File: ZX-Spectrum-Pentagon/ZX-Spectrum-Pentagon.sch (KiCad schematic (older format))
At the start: 0 parts

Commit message: improve Video_Formating
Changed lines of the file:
@@
 	7000 6500 5000 6500
 Connection ~ 5000 6500
-Wire Bus Line
-	5000 6500 5000 7750
 Wire Wire Line
 	6500 1550 6900 1550
@@
 $EndSheet
 $Sheet
-S 3500 5400 1000 2250
+S 3500 5400 1000 2200
 U 62FD43AB
 F0 "VideoFormating" 50
@@
 F8 "MD6" I L 3500 6100 50
 F9 "MD7" I L 3500 6200 50
-F10 "CBER0" I L 3500 6400 50
+F10 "CBRD0" I L 3500 6400 50
 F11 "CBRD1" I L 3500 6500 50
 F12 "CBRD2" I L 3500 6600 50
@@
 F14 "~C2" I L 3500 7000 50
 F15 "C3" I L 3500 7100 50
-F16 "C17" I L 3500 7300 50
-F17 "C18" I L 3500 7400 50
-F18 "BL" I L 3500 7500 50
+F16 "C17" I L 3500 7400 50
+F17 "C18" I L 3500 7500 50
+F18 "BL" I R 4500 7500 50
 F19 "RED" O R 4500 5600 50
 F20 "GREEN" O R 4500 5700 50
 F21 "BLUE" O R 4500 5800 50
-F22 "SYNCOUT" O R 4500 5900 50
-F23 "SYNC" O R 4500 6000 50
+F22 "SYNCOUT" O R 4500 6650 50
+F23 "SYNC" O R 4500 6750 50
 F24 "F-25Hz" I L 3500 6300 50
 F25 "PA6" I L 3500 6700 50
 F26 "PA7" I L 3500 6800 50
 F27 "C5" I L 3500 7200 50
-F28 "GPA6" O R 4500 6100 50
-F29 "GPA7" O R 4500 6200 50
+F28 "GPA6" O R 4500 7100 50
+F29 "GPA7" O R 4500 7200 50
+F30 "C7" I L 3500 7300 50
 $EndSheet
 Wire Wire Line
@@
 C3
 Text Label 3100 7300 0    50   ~ 0
+C7
+Text Label 3100 7400 0    50   ~ 0
 C17
-Text Label 3100 7400 0    50   ~ 0
+Text Label 3100 7500 0    50   ~ 0
 C18
-Text Label 3100 7500 0    50   ~ 0
-BL
 Entry Wire Line
 	5000 5700 4900 5600
@@
 	5000 5900 4900 5800
 Entry Wire Line
-	5000 6000 4900 5900
-Entry Wire Line
-	5000 6100 4900 6000
+	5000 6750 4900 6650
+Entry Wire Line
+	5000 6850 4900 6750
 Wire Wire Line
 	4900 5600 4500 5600
@@
 	4900 5800 4500 5800
 Wire Wire Line
-	4900 5900 4500 5900
-Wire Wire Line
-	4900 6000 4500 6000
+	4900 6650 4500 6650
+Wire Wire Line
+	4900 6750 4500 6750
 Text Label 4900 5600 2    50   ~ 0
 RED
@@
 Text Label 4900 5800 2    50   ~ 0
 BLUE
-Text Label 4900 5900 2    50   ~ 0
+Text Label 4900 6650 2    50   ~ 0
 SYNCOUT
-Text Label 4900 6000 2    50   ~ 0
+Text Label 4900 6750 2    50   ~ 0
 SYNC
 Entry Wire Line
@@
 C5
 Entry Wire Line
-	4900 6100 5000 6200
-Entry Wire Line
-	4900 6200 5000 6300
-Wire Wire Line
-	4500 6100 4900 6100
-Wire Wire Line
-	4500 6200 4900 6200
+	4900 7100 5000 7200
+Entry Wire Line
+	4900 7200 5000 7300
+Wire Wire Line
+	4500 7100 4900 7100
+Wire Wire Line
+	4500 7200 4900 7200
+Text Label 4900 7100 2    50   ~ 0
+GPA6
+Text Label 4900 7200 2    50   ~ 0
+GPA7
+Entry Wire Line
+	4900 7500 5000 7600
+Wire Wire Line
+	4500 7500 4900 7500
+Text Label 4900 7500 2    50   ~ 0
+BL
+Wire Bus Line
+	5000 6500 5000 7750
 Wire Bus Line
 	1000 900  1000 7750
@@
 Wire Bus Line
 	3000 800  3000 7750
-Text Label 4900 6100 2    50   ~ 0
-GPA6
-Text Label 4900 6200 2    50   ~ 0
-GPA7
 $EndSCHEMATC

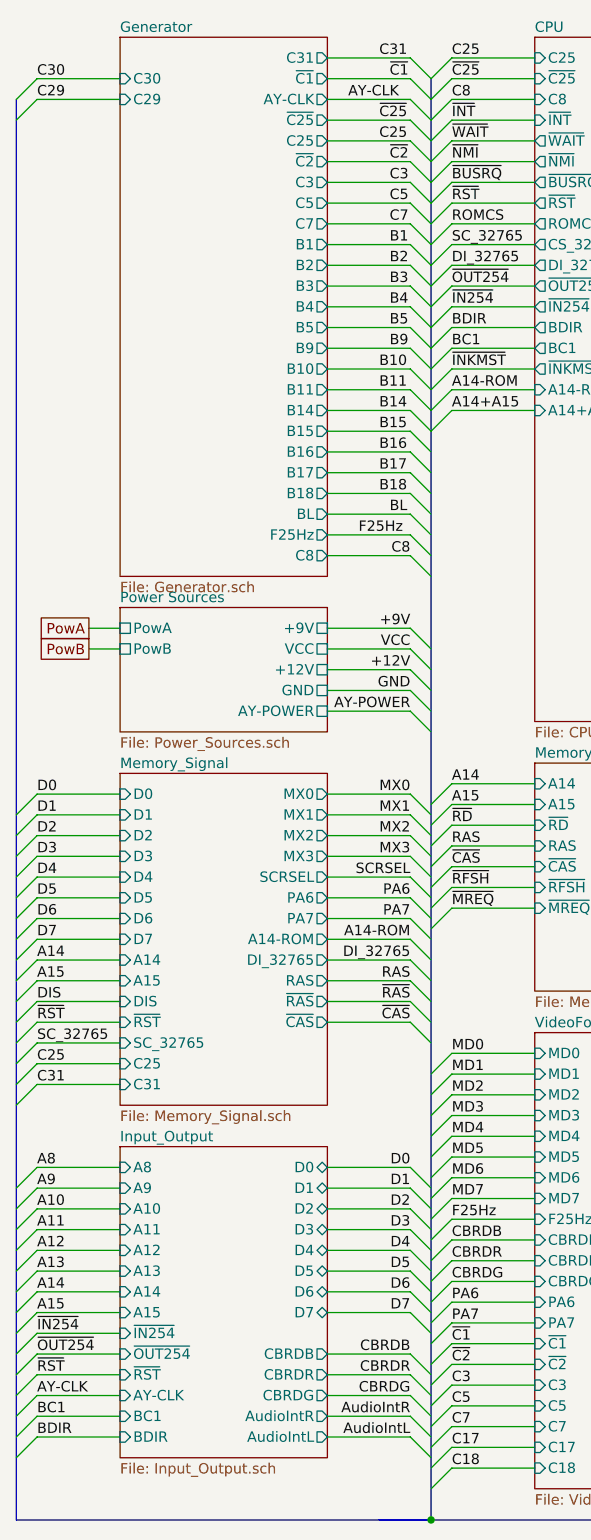
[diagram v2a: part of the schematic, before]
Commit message: add 2 signal VSYNC and HSYNC
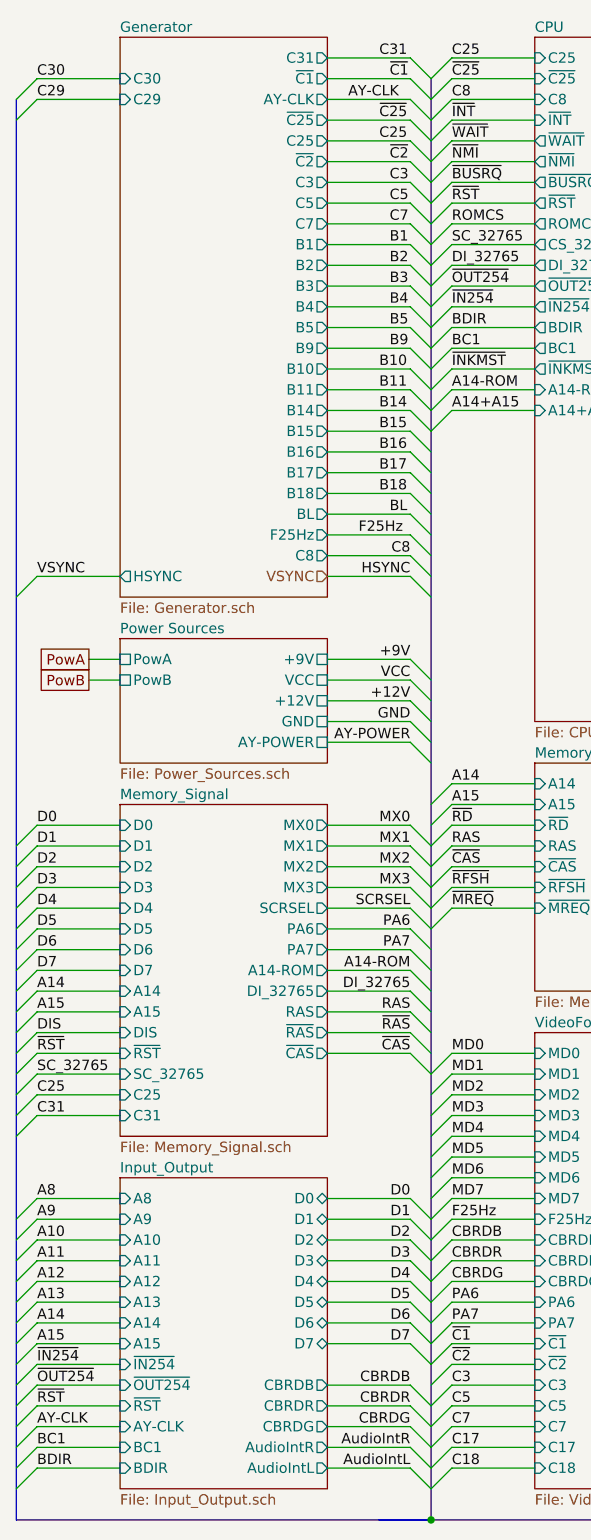
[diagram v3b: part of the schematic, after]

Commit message: reset anatation
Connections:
- no-connect marks 0 -> 1
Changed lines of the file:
@@
 F8 "AY-POWER" U R 2500 4000 50
 $EndSheet
-Text Label 2800 2900 0    50   ~ 0
+Text Label 2900 2900 2    50   ~ 0
 BL
-Text Label 2750 2800 0    50   ~ 0
+Text Label 2900 2800 2    50   ~ 0
 B18
-Text Label 2750 2700 0    50   ~ 0
+Text Label 2900 2700 2    50   ~ 0
 B17
-Text Label 2750 2600 0    50   ~ 0
+Text Label 2900 2600 2    50   ~ 0
 B16
-Text Label 2750 2500 0    50   ~ 0
+Text Label 2900 2500 2    50   ~ 0
 B15
-Text Label 2750 2400 0    50   ~ 0
+Text Label 2900 2400 2    50   ~ 0
 B14
-Text Label 2750 2300 0    50   ~ 0
+Text Label 2900 2300 2    50   ~ 0
 B11
-Text Label 2750 2200 0    50   ~ 0
+Text Label 2900 2200 2    50   ~ 0
 B10
-Text Label 2800 2100 0    50   ~ 0
+Text Label 2900 2100 2    50   ~ 0
 B9
-Text Label 2800 2000 0    50   ~ 0
+Text Label 2900 2000 2    50   ~ 0
 B5
-Text Label 2800 1900 0    50   ~ 0
+Text Label 2900 1900 2    50   ~ 0
 B4
-Text Label 2800 1800 0    50   ~ 0
+Text Label 2900 1800 2    50   ~ 0
 B3
-Text Label 2800 1700 0    50   ~ 0
+Text Label 2900 1700 2    50   ~ 0
 B2
-Text Label 2800 1600 0    50   ~ 0
+Text Label 2900 1600 2    50   ~ 0
 B1
-Text Label 2800 1500 0    50   ~ 0
-C7
-Text Label 2800 1400 0    50   ~ 0
+Text Label 2900 1500 2    50   ~ 0
+SYNC
+Text Label 2900 1400 2    50   ~ 0
 C5
-Text Label 2800 1300 0    50   ~ 0
+Text Label 2900 1300 2    50   ~ 0
 C3
-Text Label 2800 1200 0    50   ~ 0
+Text Label 2900 1200 2    50   ~ 0
 ~C2
-Text Label 2750 1100 0    50   ~ 0
+Text Label 2900 1100 2    50   ~ 0
 C25
-Text Label 2750 1000 0    50   ~ 0
+Text Label 2900 1000 2    50   ~ 0
 ~C25
-Text Label 2600 900  0    50   ~ 0
+Text Label 2900 900  2    50   ~ 0
 AY-CLK
-Text Label 2800 800  0    50   ~ 0
-~C1
-Text Label 2750 700  0    50   ~ 0
+Text Label 2900 700  2    50   ~ 0
 C31
 Text Label 2900 3100 2    50   ~ 0
 C8
-Text Label 2650 3000 0    50   ~ 0
+Text Label 2900 3000 2    50   ~ 0
 F25Hz
 Wire Wire Line
@@
 F10 "C3" O R 2500 1300 50
 F11 "C5" O R 2500 1400 50
-F12 "C7" O R 2500 1500 50
+F12 "SYNC" O R 2500 1500 50
 F13 "B1" O R 2500 1600 50
 F14 "B2" O R 2500 1700 50
@@
 F21 "BLUE_CN" O R 4500 5800 50
 F22 "SYNCOUT" O R 4500 6400 50
-F23 "SYNC" O R 4500 6500 50
+F23 "SYNCO" O R 4500 6500 50
 F24 "F25Hz" I L 3500 6300 50
 F25 "PA6" I L 3500 6700 50
@@
 F28 "GPA6" O R 4500 7100 50
 F29 "GPA7" O R 4500 7200 50
-F30 "C7" I L 3500 7300 50
+F30 "SYNC" I L 3500 7300 50
 F31 "RED_EN" O R 4500 6000 50
 F32 "GREEN_EN" O R 4500 6100 50
@@
 C3
 Text Label 3100 7300 0    50   ~ 0
-C7
+SYNC
 Text Label 3100 7400 0    50   ~ 0
 C17
@@
 SYNCOUT
 Text Label 4900 6500 2    50   ~ 0
-SYNC
+SYNCO
 Entry Wire Line
 	3000 6800 3100 6700
@@
 Entry Wire Line
 	2900 3200 3000 3300
+Text Label 2900 800  2    50   ~ 0
+~C1
+NoConn ~ 17200 9450
 Wire Bus Line
 	5000 6500 5000 7750

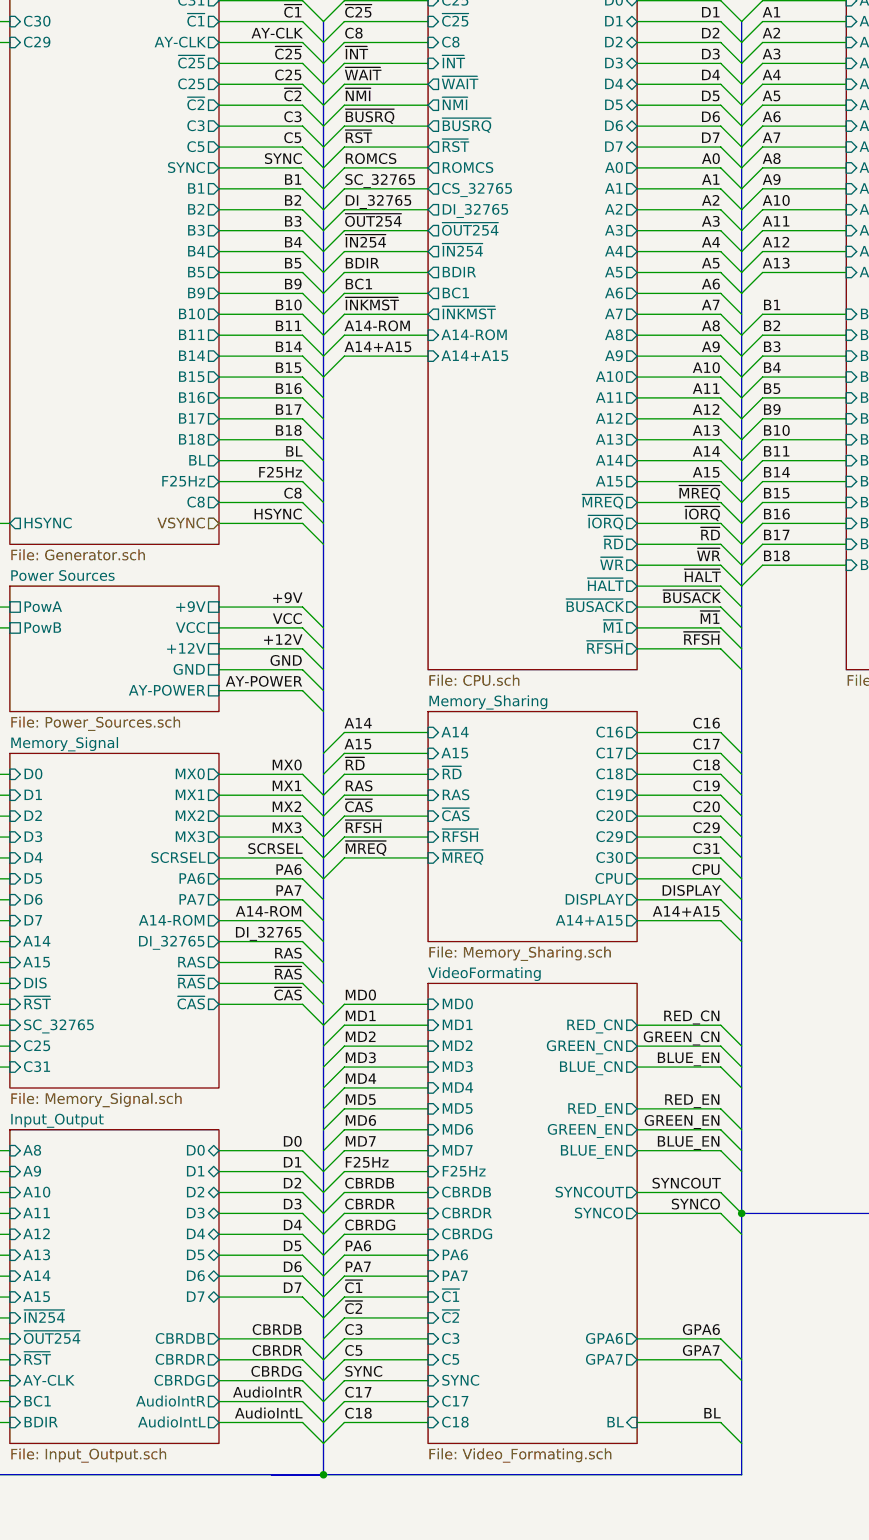
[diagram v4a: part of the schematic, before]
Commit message: rename some signals
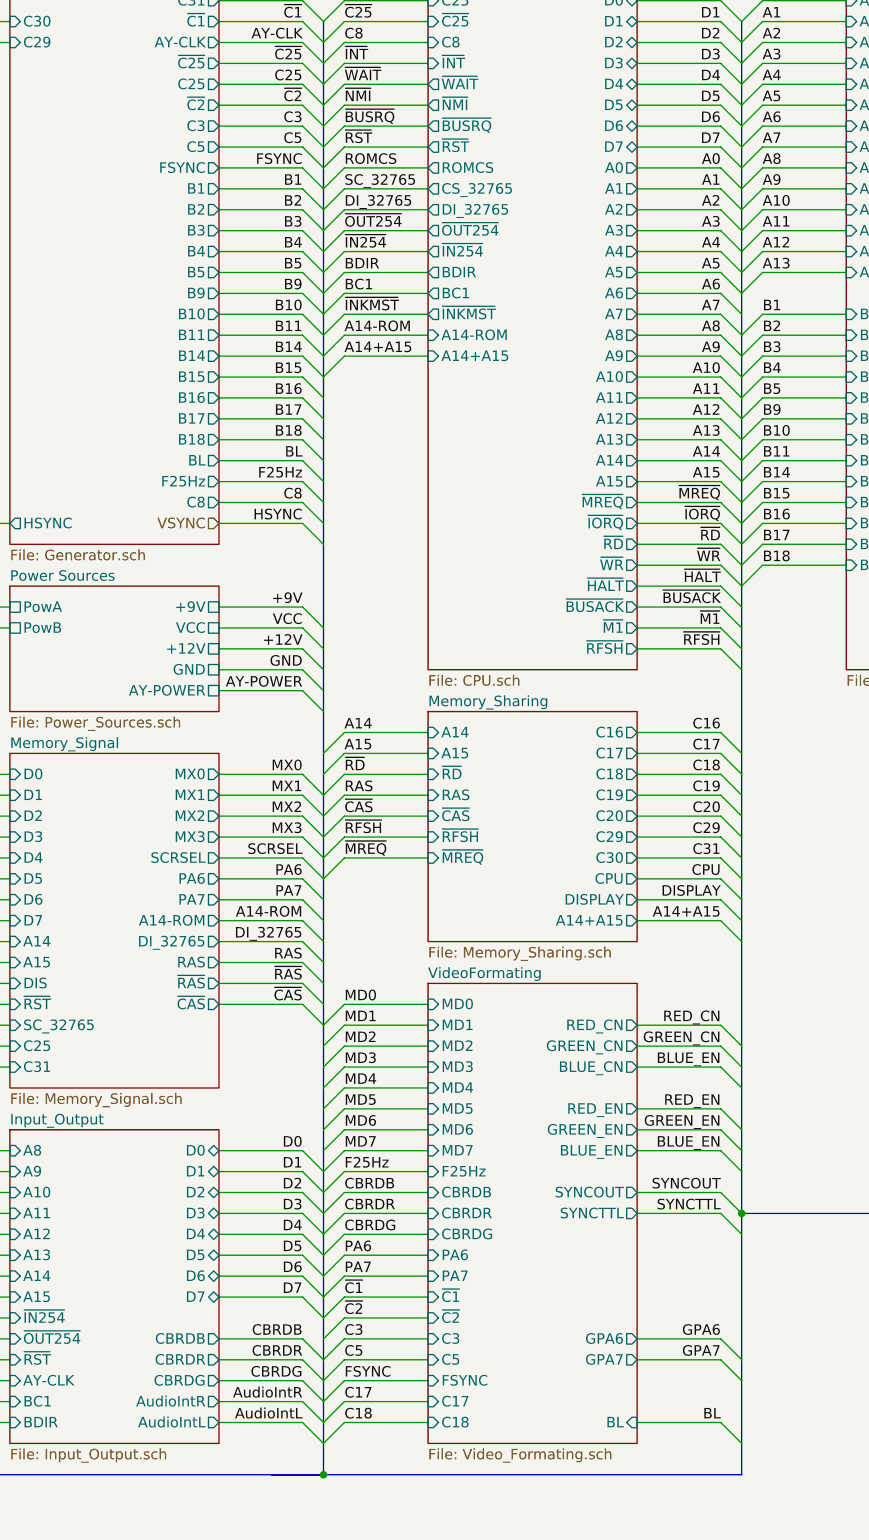
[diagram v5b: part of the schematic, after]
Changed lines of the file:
@@
 B1
 Text Label 2900 1500 2    50   ~ 0
-SYNC
+FSYNC
 Text Label 2900 1400 2    50   ~ 0
 C5
@@
 F10 "C3" O R 2500 1300 50
 F11 "C5" O R 2500 1400 50
-F12 "SYNC" O R 2500 1500 50
+F12 "FSYNC" O R 2500 1500 50
 F13 "B1" O R 2500 1600 50
 F14 "B2" O R 2500 1700 50
@@
 F21 "BLUE_CN" O R 4500 5800 50
 F22 "SYNCOUT" O R 4500 6400 50
-F23 "SYNCO" O R 4500 6500 50
+F23 "SYNCTTL" O R 4500 6500 50
 F24 "F25Hz" I L 3500 6300 50
 F25 "PA6" I L 3500 6700 50
@@
 F28 "GPA6" O R 4500 7100 50
 F29 "GPA7" O R 4500 7200 50
-F30 "SYNC" I L 3500 7300 50
+F30 "FSYNC" I L 3500 7300 50
 F31 "RED_EN" O R 4500 6000 50
 F32 "GREEN_EN" O R 4500 6100 50
@@
 C3
 Text Label 3100 7300 0    50   ~ 0
-SYNC
+FSYNC
 Text Label 3100 7400 0    50   ~ 0
 C17
@@
 SYNCOUT
 Text Label 4900 6500 2    50   ~ 0
-SYNCO
+SYNCTTL
 Entry Wire Line
 	3000 6800 3100 6700

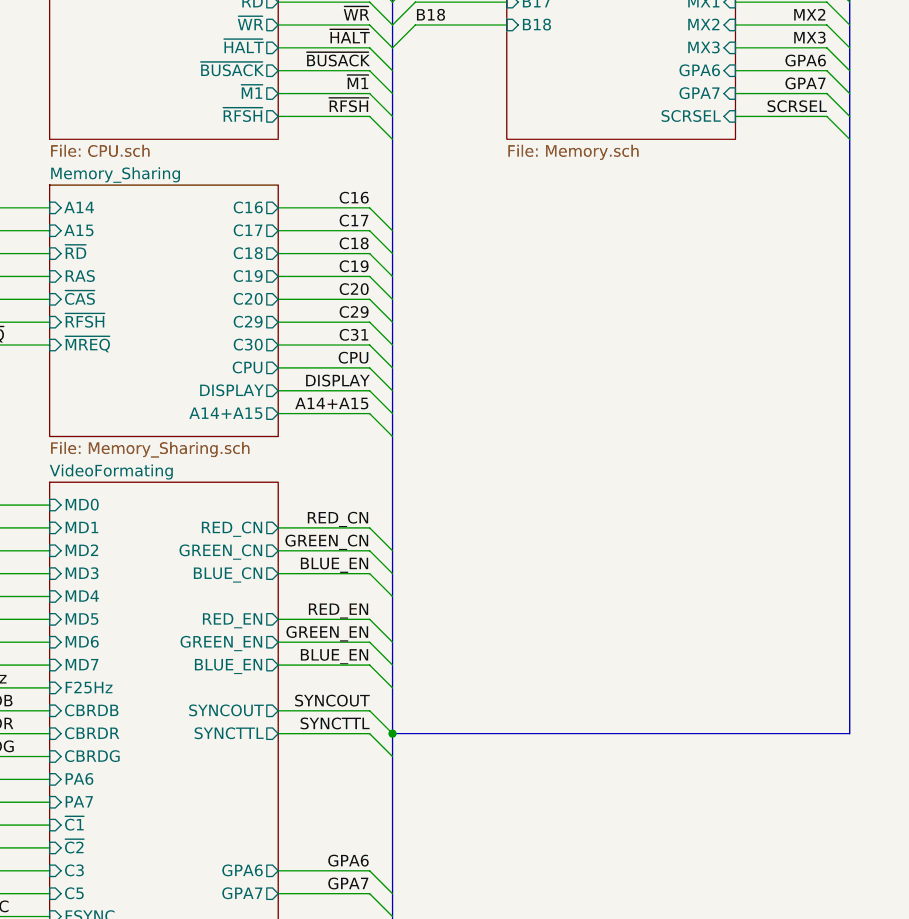
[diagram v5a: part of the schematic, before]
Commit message: add VideoEncoder sheet
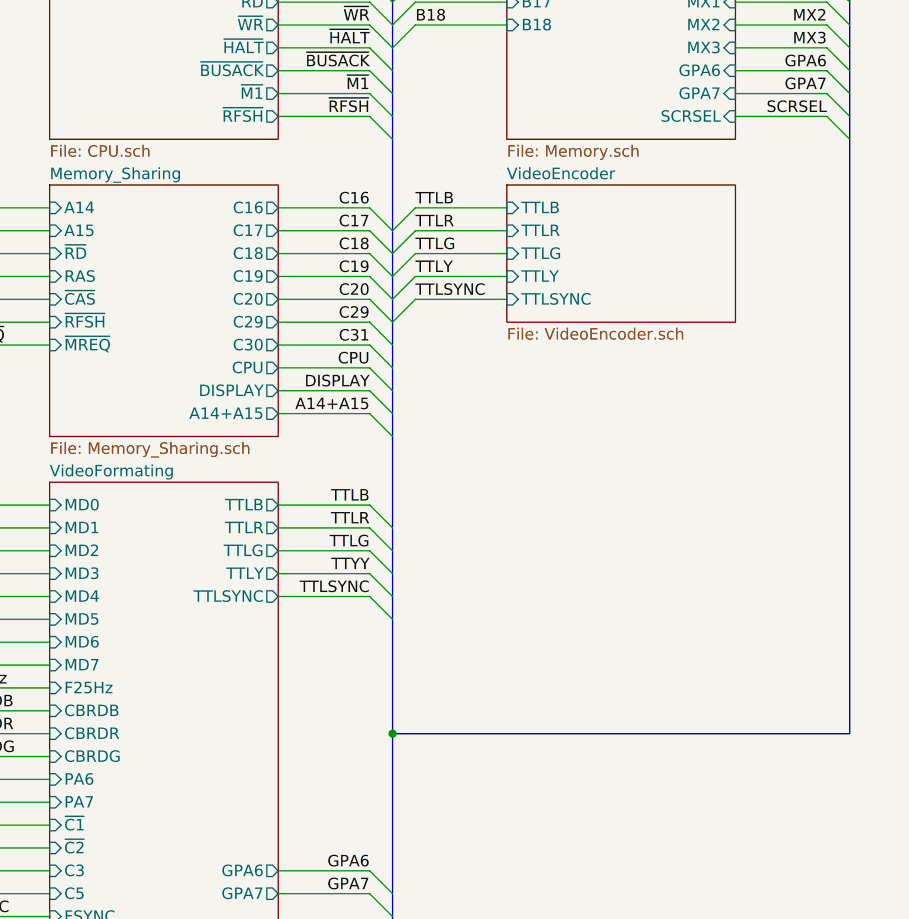
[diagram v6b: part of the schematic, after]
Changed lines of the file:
@@
 $Descr A4 11693 8268
 encoding utf-8
-Sheet 1 9
+Sheet 1 10
 Title ""
 Date ""
@@
 F17 "C18" I L 3500 7500 50
 F18 "BL" I R 4500 7500 50
-F19 "RED_CN" O R 4500 5600 50
-F20 "GREEN_CN" O R 4500 5700 50
-F21 "BLUE_CN" O R 4500 5800 50
-F22 "SYNCOUT" O R 4500 6400 50
-F23 "SYNCTTL" O R 4500 6500 50
-F24 "F25Hz" I L 3500 6300 50
-F25 "PA6" I L 3500 6700 50
-F26 "PA7" I L 3500 6800 50
-F27 "C5" I L 3500 7200 50
-F28 "GPA6" O R 4500 7100 50
-F29 "GPA7" O R 4500 7200 50
-F30 "FSYNC" I L 3500 7300 50
-F31 "RED_EN" O R 4500 6000 50
-F32 "GREEN_EN" O R 4500 6100 50
-F33 "BLUE_EN" O R 4500 6200 50
+F19 "TTLB" O R 4500 5500 50
+F20 "TTLR" O R 4500 5600 50
+F21 "TTLG" O R 4500 5700 50
+F22 "F25Hz" I L 3500 6300 50
+F23 "PA6" I L 3500 6700 50
+F24 "PA7" I L 3500 6800 50
+F25 "C5" I L 3500 7200 50
+F26 "GPA6" O R 4500 7100 50
+F27 "GPA7" O R 4500 7200 50
+F28 "FSYNC" I L 3500 7300 50
+F29 "TTLY" O R 4500 5800 50
+F30 "TTLSYNC" O R 4500 5900 50
 $EndSheet
 Wire Wire Line
@@
 C18
 Entry Wire Line
-	5000 5700 4900 5600
-Entry Wire Line
-	5000 5800 4900 5700
-Entry Wire Line
-	5000 5900 4900 5800
-Entry Wire Line
-	5000 6500 4900 6400
-Entry Wire Line
-	5000 6600 4900 6500
-Wire Wire Line
-	4900 5600 4500 5600
-Wire Wire Line
-	4900 5800 4500 5800
-Wire Wire Line
-	4900 6400 4500 6400
-Wire Wire Line
-	4900 6500 4500 6500
-Text Label 4900 5600 2    50   ~ 0
-RED_CN
-Text Label 4900 5800 2    50   ~ 0
-BLUE_EN
-Text Label 4900 6400 2    50   ~ 0
-SYNCOUT
-Text Label 4900 6500 2    50   ~ 0
-SYNCTTL
-Entry Wire Line
 	3000 6800 3100 6700
 Entry Wire Line
@@
 Text Label 4900 7500 2    50   ~ 0
 BL
-Wire Wire Line
-	4900 5700 4500 5700
-Text Label 4900 5700 2    50   ~ 0
-GREEN_CN
-Entry Wire Line
-	5000 6100 4900 6000
-Entry Wire Line
-	5000 6200 4900 6100
-Entry Wire Line
-	5000 6300 4900 6200
-Wire Wire Line
-	4900 6000 4500 6000
-Wire Wire Line
-	4900 6200 4500 6200
-Text Label 4900 6000 2    50   ~ 0
-RED_EN
-Text Label 4900 6200 2    50   ~ 0
-BLUE_EN
-Wire Wire Line
-	4900 6100 4500 6100
-Text Label 4900 6100 2    50   ~ 0
-GREEN_EN
 Entry Wire Line
 	5100 2000 5000 2100
@@
 ~C1
 NoConn ~ 17200 9450
+$Sheet
+S 5500 4100 1000 600
+U 62BF0F7B
+F0 "VideoEncoder" 50
+F1 "VideoEncoder.sch" 50
+F2 "TTLB" I L 5500 4200 50
+F3 "TTLR" I L 5500 4300 50
+F4 "TTLG" I L 5500 4400 50
+F5 "TTLY" I L 5500 4500 50
+F6 "TTLSYNC" I L 5500 4600 50
+$EndSheet
+Entry Wire Line
+	5000 4300 5100 4200
+Entry Wire Line
+	5000 4400 5100 4300
+Entry Wire Line
+	5000 4500 5100 4400
+Wire Wire Line
+	5100 4200 5500 4200
+Wire Wire Line
+	5100 4400 5500 4400
+Text Label 5100 4200 0    50   ~ 0
+TTLB
+Text Label 5100 4400 0    50   ~ 0
+TTLG
+Wire Wire Line
+	5100 4300 5500 4300
+Text Label 5100 4300 0    50   ~ 0
+TTLR
+Entry Wire Line
+	5000 4600 5100 4500
+Entry Wire Line
+	5000 4700 5100 4600
+Wire Wire Line
+	5100 4500 5500 4500
+Text Label 5100 4500 0    50   ~ 0
+TTLY
+Wire Wire Line
+	5100 4600 5500 4600
+Text Label 5100 4600 0    50   ~ 0
+TTLSYNC
+Entry Wire Line
+	5000 6000 4900 5900
+Entry Wire Line
+	5000 5900 4900 5800
+Entry Wire Line
+	5000 5800 4900 5700
+Entry Wire Line
+	5000 5700 4900 5600
+Entry Wire Line
+	5000 5600 4900 5500
+Wire Wire Line
+	4900 5500 4500 5500
+Wire Wire Line
+	4900 5700 4500 5700
+Text Label 4900 5500 2    50   ~ 0
+TTLB
+Text Label 4900 5700 2    50   ~ 0
+TTLG
+Wire Wire Line
+	4900 5600 4500 5600
+Text Label 4900 5600 2    50   ~ 0
+TTLR
+Wire Wire Line
+	4900 5800 4500 5800
+Text Label 4900 5800 2    50   ~ 0
+TTYY
+Wire Wire Line
+	4900 5900 4500 5900
+Text Label 4900 5900 2    50   ~ 0
+TTLSYNC
 Wire Bus Line
 	5000 6500 5000 7750
